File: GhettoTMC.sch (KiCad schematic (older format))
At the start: 36 parts

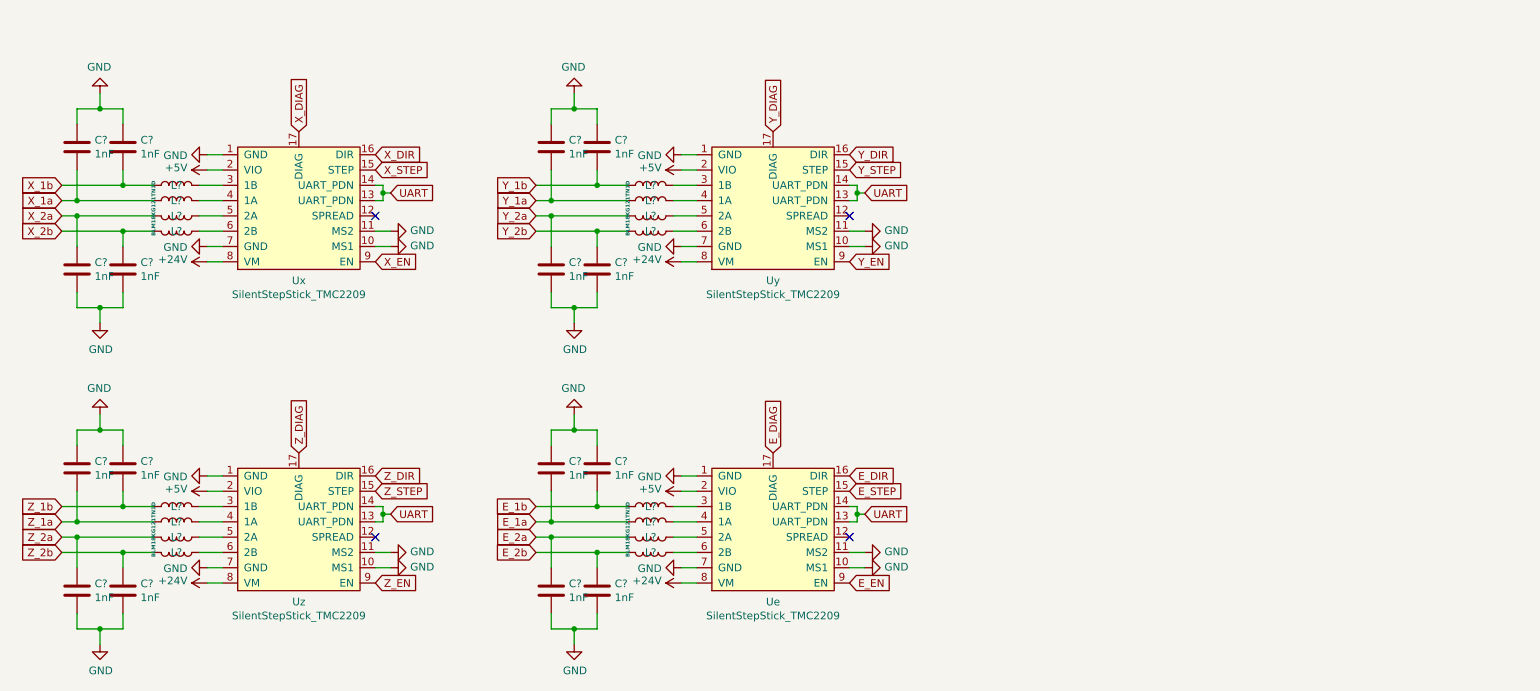
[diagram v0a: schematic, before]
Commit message: Add Stepper connectors
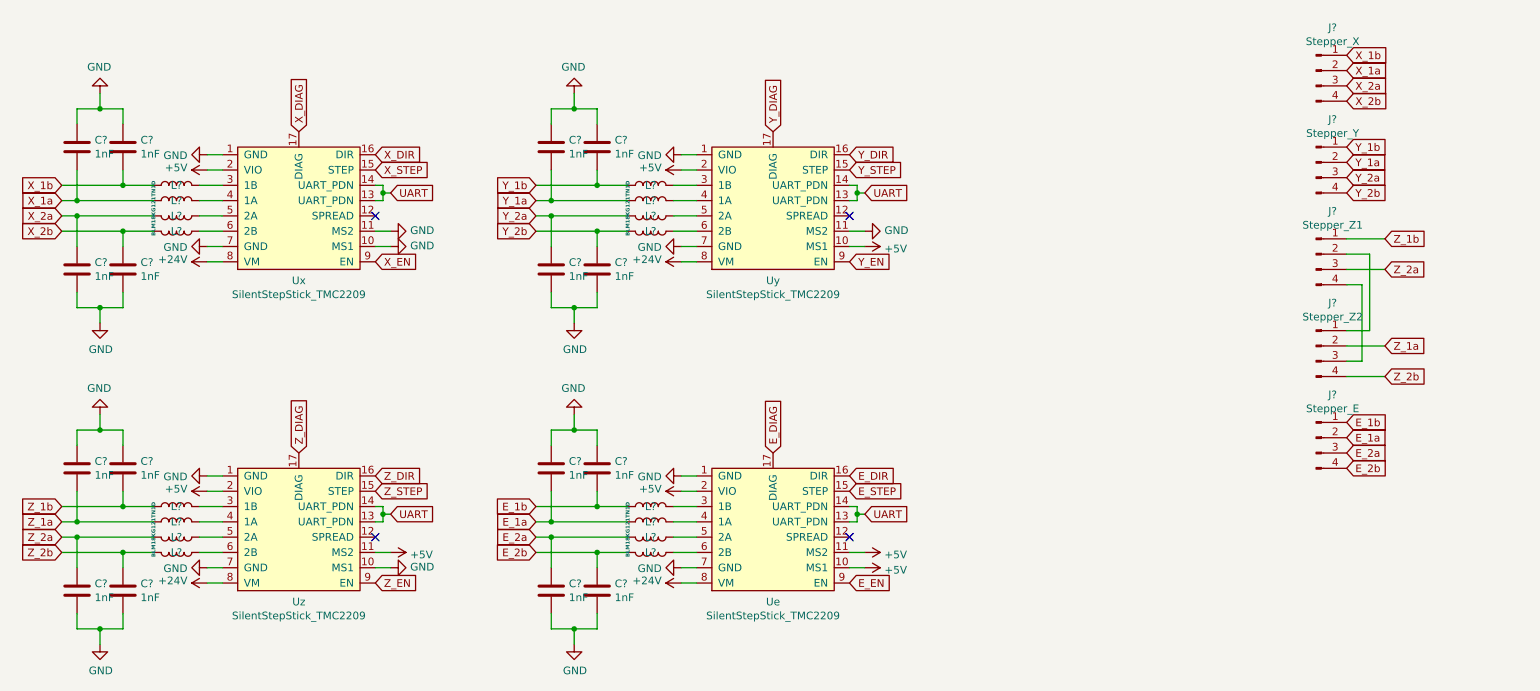
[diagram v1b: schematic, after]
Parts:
- added J?: Stepper_X, symbol Connector:Conn_01x04_Male
- added J?: Stepper_Y, symbol Connector:Conn_01x04_Male
- added J?: Stepper_Z1, symbol Connector:Conn_01x04_Male
- added J?: Stepper_Z2, symbol Connector:Conn_01x04_Male
- added J?: Stepper_E, symbol Connector:Conn_01x04_Male
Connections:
- net +5V: now also Ue.10 (MS1), Ue.11 (MS2), Uy.10 (MS1), Uz.11 (MS2)
- net E_1a: now also J?.2 (Pin_2)
- net E_1b: now also J?.1 (Pin_1)
- net E_2a: now also J?.3 (Pin_3)
- net E_2b: now also J?.4 (Pin_4)
- net GND: no longer Ue.10 (MS1), Ue.11 (MS2), Uy.10 (MS1), Uz.11 (MS2)
- net X_1a: now also J?.2 (Pin_2)
- net X_1b: now also J?.1 (Pin_1)
- net X_2a: now also J?.3 (Pin_3)
- net X_2b: now also J?.4 (Pin_4)
- net Y_1a: now also J?.2 (Pin_2)
- net Y_1b: now also J?.1 (Pin_1)
- net Y_2a: now also J?.3 (Pin_3)
- net Y_2b: now also J?.4 (Pin_4)
- net Z_1a: now also J?.2 (Pin_2)
- net Z_1b: now also J?.1 (Pin_1)
- net Z_2a: now also J?.3 (Pin_3)
- net Z_2b: now also J?.4 (Pin_4)
- new net: J?.1 (Pin_1), J?.2 (Pin_2)
- new net: J?.3 (Pin_3), J?.4 (Pin_4)
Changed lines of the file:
@@
-	0    -1   -1   0
-$EndComp
-$Comp
-L power:GND #PWR?
-U 1 1 5EA23985
-P 6200 2300
-F 0 "#PWR?" H 6200 2050 50  0001 C CNN
-F 1 "GND" V 6205 2172 50  0000 R CNN
-F 2 "" H 6200 2300 50  0001 C CNN
-F 3 "" H 6200 2300 50  0001 C CNN
-	1    6200 2300
 	0    -1   -1   0
 $EndComp
@@
 $Comp
 L power:GND #PWR?
-U 1 1 5EAD959C
-P 3100 4300
-F 0 "#PWR?" H 3100 4050 50  0001 C CNN
-F 1 "GND" V 3105 4172 50  0000 R CNN
-F 2 "" H 3100 4300 50  0001 C CNN
-F 3 "" H 3100 4300 50  0001 C CNN
-	1    3100 4300
-	0    -1   -1   0
-$EndComp
-$Comp
-L power:GND #PWR?
 U 1 1 5EAD95A2
 P 3100 4400
@@
 	0    1    1    0
 $EndComp
-$Comp
-L power:GND #PWR?
-U 1 1 5EAD9638
-P 6200 4300
-F 0 "#PWR?" H 6200 4050 50  0001 C CNN
-F 1 "GND" V 6205 4172 50  0000 R CNN
-F 2 "" H 6200 4300 50  0001 C CNN
-F 3 "" H 6200 4300 50  0001 C CNN
-	1    6200 4300
-	0    -1   -1   0
-$EndComp
-$Comp
-L power:GND #PWR?
-U 1 1 5EAD963E
-P 6200 4400
-F 0 "#PWR?" H 6200 4150 50  0001 C CNN
-F 1 "GND" V 6205 4272 50  0000 R CNN
-F 2 "" H 6200 4400 50  0001 C CNN
-F 3 "" H 6200 4400 50  0001 C CNN
-	1    6200 4400
-	0    -1   -1   0
-$EndComp
 Wire Wire Line
 	6200 4400 6100 4400
@@
 	1    0    0    -1
 $EndComp
+$Comp
+L power:+5V #PWR?
+U 1 1 5E9E3D53
+P 6200 2300
+F 0 "#PWR?" H 6200 2150 50  0001 C CNN
+F 1 "+5V" V 6215 2428 50  0000 L CNN
+F 2 "" H 6200 2300 50  0001 C CNN
+F 3 "" H 6200 2300 50  0001 C CNN
+	1    6200 2300
+	0    1    1    0
+$EndComp
+$Comp
+L power:+5V #PWR?
+U 1 1 5E9E465C
+P 6200 4300
+F 0 "#PWR?" H 6200 4150 50  0001 C CNN
+F 1 "+5V" V 6215 4428 50  0000 L CNN
+F 2 "" H 6200 4300 50  0001 C CNN
+F 3 "" H 6200 4300 50  0001 C CNN
+	1    6200 4300
+	0    1    1    0
+$EndComp
+$Comp
+L power:+5V #PWR?
+U 1 1 5E9EBC6F
+P 6200 4400
+F 0 "#PWR?" H 6200 4250 50  0001 C CNN
+F 1 "+5V" V 6215 4528 50  0000 L CNN
+F 2 "" H 6200 4400 50  0001 C CNN
+F 3 "" H 6200 4400 50  0001 C CNN
+	1    6200 4400
+	0    1    1    0
+$EndComp
+$Comp
+L power:+5V #PWR?
+U 1 1 5EA06571
+P 3100 4300
+F 0 "#PWR?" H 3100 4150 50  0001 C CNN
+F 1 "+5V" V 3115 4428 50  0000 L CNN
+F 2 "" H 3100 4300 50  0001 C CNN
+F 3 "" H 3100 4300 50  0001 C CNN
+	1    3100 4300
+	0    1    1    0
+$EndComp
+$Comp
+L Connector:Conn_01x04_Male J?
+U 1 1 5EA0E71E
+P 9150 1150
+F 0 "J?" H 9258 1431 50  0000 C CNN
+F 1 "Stepper_X" H 9258 1340 50  0000 C CNN
+F 2 "" H 9150 1150 50  0001 C CNN
+F 3 "~" H 9150 1150 50  0001 C CNN
+	1    9150 1150
+	1    0    0    -1
+$EndComp
+$Comp
+L Connector:Conn_01x04_Male J?
+U 1 1 5EA10DB0
+P 9150 1750
+F 0 "J?" H 9258 2031 50  0000 C CNN
+F 1 "Stepper_Y" H 9258 1940 50  0000 C CNN
+F 2 "" H 9150 1750 50  0001 C CNN
+F 3 "~" H 9150 1750 50  0001 C CNN
+	1    9150 1750
+	1    0    0    -1
+$EndComp
+$Comp
+L Connector:Conn_01x04_Male J?
+U 1 1 5EA11A2D
+P 9150 2350
+F 0 "J?" H 9258 2631 50  0000 C CNN
+F 1 "Stepper_Z1" H 9258 2540 50  0000 C CNN
+F 2 "" H 9150 2350 50  0001 C CNN
+F 3 "~" H 9150 2350 50  0001 C CNN
+	1    9150 2350
+	1    0    0    -1
+$EndComp
+$Comp
+L Connector:Conn_01x04_Male J?
+U 1 1 5EA12536
+P 9150 2950
+F 0 "J?" H 9258 3231 50  0000 C CNN
+F 1 "Stepper_Z2" H 9258 3140 50  0000 C CNN
+F 2 "" H 9150 2950 50  0001 C CNN
+F 3 "~" H 9150 2950 50  0001 C CNN
+	1    9150 2950
+	1    0    0    -1
+$EndComp
+$Comp
+L Connector:Conn_01x04_Male J?
+U 1 1 5EA14BF3
+P 9150 3550
+F 0 "J?" H 9258 3831 50  0000 C CNN
+F 1 "Stepper_E" H 9258 3740 50  0000 C CNN
+F 2 "" H 9150 3550 50  0001 C CNN
+F 3 "~" H 9150 3550 50  0001 C CNN
+	1    9150 3550
+	1    0    0    -1
+$EndComp
+Wire Wire Line
+	9350 2350 9500 2350
+Wire Wire Line
+	9500 2350 9500 2850
+Wire Wire Line
+	9500 2850 9350 2850
+Wire Wire Line
+	9350 2550 9450 2550
+Wire Wire Line
+	9450 2550 9450 3050
+Wire Wire Line
+	9450 3050 9350 3050
+Wire Wire Line
+	9350 3150 9600 3150
+Wire Wire Line
+	9350 2950 9600 2950
+Wire Wire Line
+	9350 2450 9600 2450
+Wire Wire Line
+	9350 2250 9600 2250
+Text GLabel 9350 1050 2    50   Input ~ 0
+X_1b
+Text GLabel 9350 1750 2    50   Input ~ 0
+Y_1a
+Text GLabel 9350 1850 2    50   Input ~ 0
+Y_2a
+Text GLabel 9350 1950 2    50   Input ~ 0
+Y_2b
+Text GLabel 9350 1650 2    50   Input ~ 0
+Y_1b
+Text GLabel 9350 1150 2    50   Input ~ 0
+X_1a
+Text GLabel 9350 1250 2    50   Input ~ 0
+X_2a
+Text GLabel 9350 1350 2    50   Input ~ 0
+X_2b
+Text GLabel 9350 3550 2    50   Input ~ 0
+E_1a
+Text GLabel 9350 3650 2    50   Input ~ 0
+E_2a
+Text GLabel 9350 3750 2    50   Input ~ 0
+E_2b
+Text GLabel 9350 3450 2    50   Input ~ 0
+E_1b
+Text GLabel 9600 2950 2    50   Input ~ 0
+Z_1a
+Text GLabel 9600 2450 2    50   Input ~ 0
+Z_2a
+Text GLabel 9600 3150 2    50   Input ~ 0
+Z_2b
+Text GLabel 9600 2250 2    50   Input ~ 0
+Z_1b
 $EndSCHEMATC

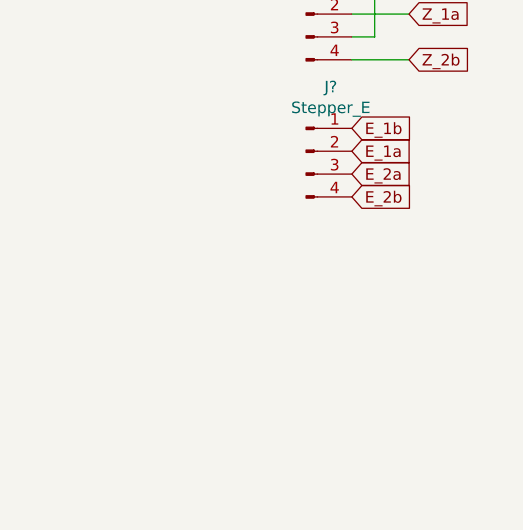
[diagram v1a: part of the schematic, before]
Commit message: Add Data connector
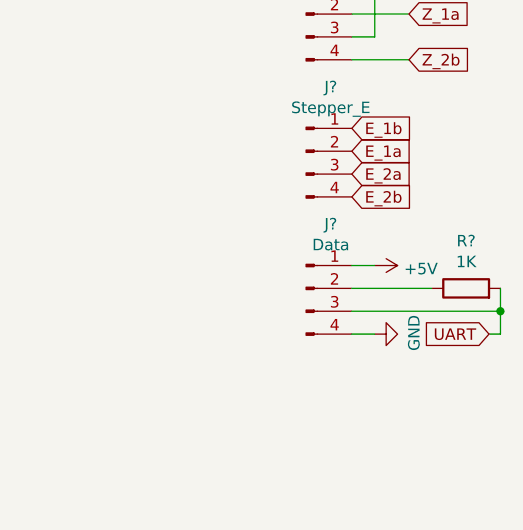
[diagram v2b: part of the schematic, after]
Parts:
- added J?: Data, GhettoTMC:MOLEX_70553-0038, symbol Connector:Conn_01x04_Male
- added R?: 1K, symbol Device:R
- J? (x5): footprint (none) -> GhettoTMC:MOLEX_70553-0038
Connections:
- net +5V: now also J?.1 (Pin_1)
- net GND: now also J?.4 (Pin_4)
- net UART: now also J?.3 (Pin_3), R?.2
- new net: J?.2 (Pin_2), R?.1
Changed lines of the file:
@@
 F 0 "J?" H 9258 1431 50  0000 C CNN
 F 1 "Stepper_X" H 9258 1340 50  0000 C CNN
-F 2 "" H 9150 1150 50  0001 C CNN
+F 2 "GhettoTMC:MOLEX_70553-0038" H 9150 1150 50  0001 C CNN
 F 3 "~" H 9150 1150 50  0001 C CNN
 	1    9150 1150
@@
 F 0 "J?" H 9258 2031 50  0000 C CNN
 F 1 "Stepper_Y" H 9258 1940 50  0000 C CNN
-F 2 "" H 9150 1750 50  0001 C CNN
+F 2 "GhettoTMC:MOLEX_70553-0038" H 9150 1750 50  0001 C CNN
 F 3 "~" H 9150 1750 50  0001 C CNN
 	1    9150 1750
@@
 F 0 "J?" H 9258 2631 50  0000 C CNN
 F 1 "Stepper_Z1" H 9258 2540 50  0000 C CNN
-F 2 "" H 9150 2350 50  0001 C CNN
+F 2 "GhettoTMC:MOLEX_70553-0038" H 9150 2350 50  0001 C CNN
 F 3 "~" H 9150 2350 50  0001 C CNN
 	1    9150 2350
@@
 F 0 "J?" H 9258 3231 50  0000 C CNN
 F 1 "Stepper_Z2" H 9258 3140 50  0000 C CNN
-F 2 "" H 9150 2950 50  0001 C CNN
+F 2 "GhettoTMC:MOLEX_70553-0038" H 9150 2950 50  0001 C CNN
 F 3 "~" H 9150 2950 50  0001 C CNN
 	1    9150 2950
@@
 F 0 "J?" H 9258 3831 50  0000 C CNN
 F 1 "Stepper_E" H 9258 3740 50  0000 C CNN
-F 2 "" H 9150 3550 50  0001 C CNN
+F 2 "GhettoTMC:MOLEX_70553-0038" H 9150 3550 50  0001 C CNN
 F 3 "~" H 9150 3550 50  0001 C CNN
 	1    9150 3550
@@
 Text GLabel 9600 2250 2    50   Input ~ 0
 Z_1b
+$Comp
+L Connector:Conn_01x04_Male J?
+U 1 1 5EA64F35
+P 9150 4150
+F 0 "J?" H 9258 4431 50  0000 C CNN
+F 1 "Data" H 9258 4340 50  0000 C CNN
+F 2 "GhettoTMC:MOLEX_70553-0038" H 9150 4150 50  0001 C CNN
+F 3 "~" H 9150 4150 50  0001 C CNN
+	1    9150 4150
+	1    0    0    -1
+$EndComp
+$Comp
+L power:GND #PWR?
+U 1 1 5EA6F9F9
+P 9450 4350
+F 0 "#PWR?" H 9450 4100 50  0001 C CNN
+F 1 "GND" H 9455 4177 50  0000 C CNN
+F 2 "" H 9450 4350 50  0001 C CNN
+F 3 "" H 9450 4350 50  0001 C CNN
+	1    9450 4350
+	0    -1   -1   0
+$EndComp
+$Comp
+L power:+5V #PWR?
+U 1 1 5EA70386
+P 9450 4050
+F 0 "#PWR?" H 9450 3900 50  0001 C CNN
+F 1 "+5V" V 9465 4178 50  0000 L CNN
+F 2 "" H 9450 4050 50  0001 C CNN
+F 3 "" H 9450 4050 50  0001 C CNN
+	1    9450 4050
+	0    1    1    0
+$EndComp
+Wire Wire Line
+	9350 4050 9450 4050
+Wire Wire Line
+	9450 4350 9350 4350
+$Comp
+L Device:R R?
+U 1 1 5EA8AE5C
+P 9850 4150
+F 0 "R?" V 10057 4150 50  0000 C CNN
+F 1 "1K" V 9966 4150 50  0000 C CNN
+F 2 "" V 9780 4150 50  0001 C CNN
+F 3 "~" H 9850 4150 50  0001 C CNN
+	1    9850 4150
+	0    -1   -1   0
+$EndComp
+Wire Wire Line
+	9700 4150 9350 4150
+Wire Wire Line
+	9350 4250 10000 4250
+Wire Wire Line
+	10000 4250 10000 4150
+Text GLabel 9950 4350 0    50   Input ~ 0
+UART
+Wire Wire Line
+	9950 4350 10000 4350
+Wire Wire Line
+	10000 4350 10000 4250
+Connection ~ 10000 4250
 $EndSCHEMATC

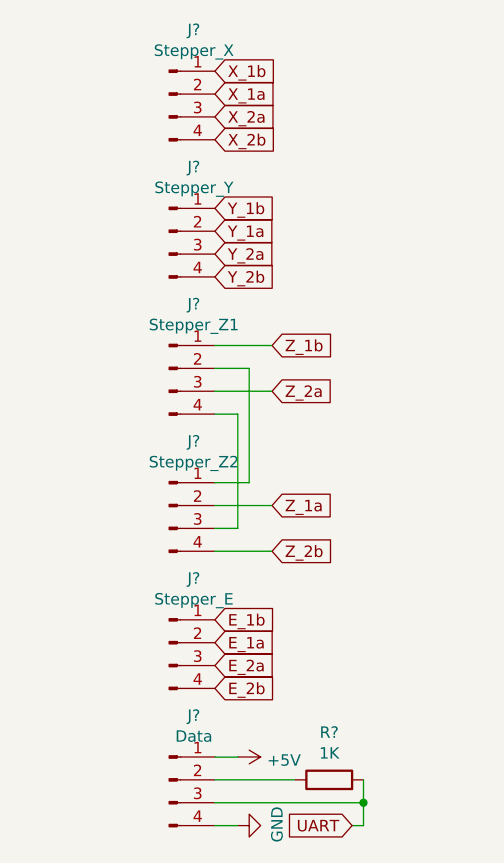
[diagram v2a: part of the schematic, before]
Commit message: Add Board connectors
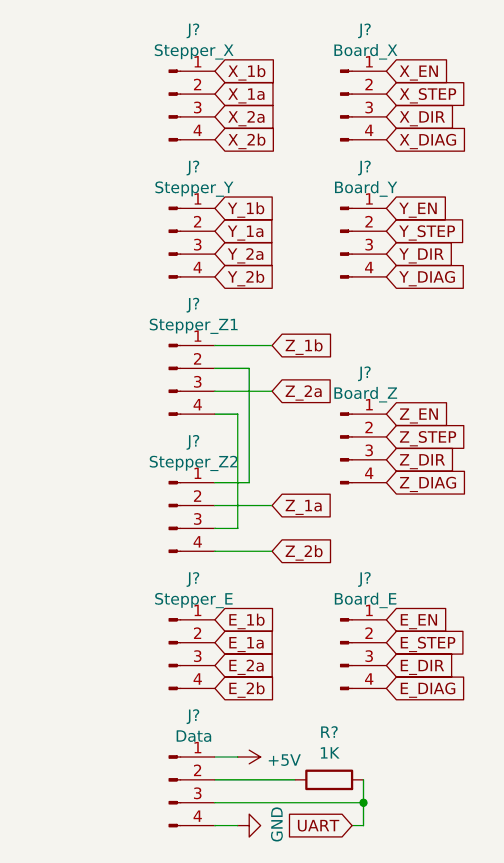
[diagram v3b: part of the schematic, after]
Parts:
- added J?: Board_Y, GhettoTMC:MOLEX_70553-0038, symbol Connector:Conn_01x04_Male
- added J?: Board_X, GhettoTMC:MOLEX_70553-0038, symbol Connector:Conn_01x04_Male
- added J?: Board_Z, GhettoTMC:MOLEX_70553-0038, symbol Connector:Conn_01x04_Male
- added J?: Board_E, GhettoTMC:MOLEX_70553-0038, symbol Connector:Conn_01x04_Male
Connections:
- net E_DIAG: now also J?.4 (Pin_4)
- net E_DIR: now also J?.3 (Pin_3)
- net E_EN: now also J?.1 (Pin_1)
- net E_STEP: now also J?.2 (Pin_2)
- net X_DIAG: now also J?.4 (Pin_4)
- net X_DIR: now also J?.3 (Pin_3)
- net X_EN: now also J?.1 (Pin_1)
- net X_STEP: now also J?.2 (Pin_2)
- net Y_DIAG: now also J?.4 (Pin_4)
- net Y_DIR: now also J?.3 (Pin_3)
- net Y_EN: now also J?.1 (Pin_1)
- net Y_STEP: now also J?.2 (Pin_2)
- net Z_DIAG: now also J?.4 (Pin_4)
- net Z_DIR: now also J?.3 (Pin_3)
- net Z_EN: now also J?.1 (Pin_1)
- net Z_STEP: now also J?.2 (Pin_2)
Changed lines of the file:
@@
 	10000 4350 10000 4250
 Connection ~ 10000 4250
+$Comp
+L Connector:Conn_01x04_Male J?
+U 1 1 5EAC38CC
+P 9900 1750
+F 0 "J?" H 10008 2031 50  0000 C CNN
+F 1 "Board_Y" H 10008 1940 50  0000 C CNN
+F 2 "GhettoTMC:MOLEX_70553-0038" H 9900 1750 50  0001 C CNN
+F 3 "~" H 9900 1750 50  0001 C CNN
+	1    9900 1750
+	1    0    0    -1
+$EndComp
+$Comp
+L Connector:Conn_01x04_Male J?
+U 1 1 5EAC4D8C
+P 9900 1150
+F 0 "J?" H 10008 1431 50  0000 C CNN
+F 1 "Board_X" H 10008 1340 50  0000 C CNN
+F 2 "GhettoTMC:MOLEX_70553-0038" H 9900 1150 50  0001 C CNN
+F 3 "~" H 9900 1150 50  0001 C CNN
+	1    9900 1150
+	1    0    0    -1
+$EndComp
+$Comp
+L Connector:Conn_01x04_Male J?
+U 1 1 5EAC51EC
+P 9900 2650
+F 0 "J?" H 10008 2931 50  0000 C CNN
+F 1 "Board_Z" H 10008 2840 50  0000 C CNN
+F 2 "GhettoTMC:MOLEX_70553-0038" H 9900 2650 50  0001 C CNN
+F 3 "~" H 9900 2650 50  0001 C CNN
+	1    9900 2650
+	1    0    0    -1
+$EndComp
+$Comp
+L Connector:Conn_01x04_Male J?
+U 1 1 5EAC5E5C
+P 9900 3550
+F 0 "J?" H 10008 3831 50  0000 C CNN
+F 1 "Board_E" H 10008 3740 50  0000 C CNN
+F 2 "GhettoTMC:MOLEX_70553-0038" H 9900 3550 50  0001 C CNN
+F 3 "~" H 9900 3550 50  0001 C CNN
+	1    9900 3550
+	1    0    0    -1
+$EndComp
+Text GLabel 10100 1950 2    50   Input ~ 0
+Y_DIAG
+Text GLabel 10100 1850 2    50   Input ~ 0
+Y_DIR
+Text GLabel 10100 1650 2    50   Input ~ 0
+Y_EN
+Text GLabel 10100 1750 2    50   Input ~ 0
+Y_STEP
+Text GLabel 10100 1350 2    50   Input ~ 0
+X_DIAG
+Text GLabel 10100 1250 2    50   Input ~ 0
+X_DIR
+Text GLabel 10100 1050 2    50   Input ~ 0
+X_EN
+Text GLabel 10100 1150 2    50   Input ~ 0
+X_STEP
+Text GLabel 10100 2850 2    50   Input ~ 0
+Z_DIAG
+Text GLabel 10100 2750 2    50   Input ~ 0
+Z_DIR
+Text GLabel 10100 2550 2    50   Input ~ 0
+Z_EN
+Text GLabel 10100 2650 2    50   Input ~ 0
+Z_STEP
+Text GLabel 10100 3750 2    50   Input ~ 0
+E_DIAG
+Text GLabel 10100 3650 2    50   Input ~ 0
+E_DIR
+Text GLabel 10100 3450 2    50   Input ~ 0
+E_EN
+Text GLabel 10100 3550 2    50   Input ~ 0
+E_STEP
 $EndSCHEMATC

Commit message: POWER IN
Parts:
- added J?: POWER IN, symbol Connector:Conn_01x02_Male
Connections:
- net +24V: now also J?.1 (Pin_1)
- net GND: now also J?.2 (Pin_2)
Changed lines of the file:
@@
-$EndComp
-$Comp
-L power:GND #PWR?
-U 1 1 5EA6F9F9
-P 9450 4350
-F 0 "#PWR?" H 9450 4100 50  0001 C CNN
-F 1 "GND" H 9455 4177 50  0000 C CNN
-F 2 "" H 9450 4350 50  0001 C CNN
-F 3 "" H 9450 4350 50  0001 C CNN
-	1    9450 4350
-	0    -1   -1   0
 $EndComp
 $Comp
@@
 Text GLabel 10100 3550 2    50   Input ~ 0
 E_STEP
+$Comp
+L Connector:Conn_01x02_Male J?
+U 1 1 5EAE4A69
+P 9150 4800
+F 0 "J?" H 9258 4981 50  0000 C CNN
+F 1 "POWER IN" H 9258 4890 50  0000 C CNN
+F 2 "" H 9150 4800 50  0001 C CNN
+F 3 "~" H 9150 4800 50  0001 C CNN
+	1    9150 4800
+	1    0    0    -1
+$EndComp
+$Comp
+L power:+24V #PWR?
+U 1 1 5EAE5F99
+P 9550 4800
+F 0 "#PWR?" H 9550 4650 50  0001 C CNN
+F 1 "+24V" V 9565 4928 50  0000 L CNN
+F 2 "" H 9550 4800 50  0001 C CNN
+F 3 "" H 9550 4800 50  0001 C CNN
+	1    9550 4800
+	1    0    0    -1
+$EndComp
+Wire Wire Line
+	9550 4800 9350 4800
+$Comp
+L power:GND #PWR?
+U 1 1 5EA6F9F9
+P 9450 4350
+F 0 "#PWR?" H 9450 4100 50  0001 C CNN
+F 1 "GND" H 9455 4177 50  0000 C CNN
+F 2 "" H 9450 4350 50  0001 C CNN
+F 3 "" H 9450 4350 50  0001 C CNN
+	1    9450 4350
+	0    -1   -1   0
+$EndComp
+Wire Wire Line
+	9350 4900 9550 4900
+$Comp
+L power:GND #PWR?
+U 1 1 5EAFED4F
+P 9550 4900
+F 0 "#PWR?" H 9550 4650 50  0001 C CNN
+F 1 "GND" H 9555 4727 50  0000 C CNN
+F 2 "" H 9550 4900 50  0001 C CNN
+F 3 "" H 9550 4900 50  0001 C CNN
+	1    9550 4900
+	1    0    0    -1
+$EndComp
 $EndSCHEMATC
